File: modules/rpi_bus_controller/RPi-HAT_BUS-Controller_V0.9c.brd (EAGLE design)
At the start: 65 x 56 mm, 77 parts, among them IC1 MC34063AD, IC2 ADUM1201ARZ, IC3 P89LPC922FDH,512FDH, IC4 24LC-I/OT, IC5 LPC1115, Q1 ASF1, Q4 ASFL, T1 BC856, T2 BCP52, T3 BC847

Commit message: Finalize Raspi HAT Dual MCU board
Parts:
- removed C11: 10n, rcl:C1206
- removed C15: 100n, rcl:C1206
- added C51: 10n, rcl:C1206
- added C55: 100n, rcl:C1206
- moved C8 0.15 mm to (11.9, 14.6)
- renumbered C12 to C52, C13 to C53, C14 to C54, C20 to C50, C21 to C56, C22 to C57, D10 to D51, D9 to D50, R21 to R51, R22 to R52, R23 to R53, R24 to R54, R28 to R58, R29 to R59, R30 to R50
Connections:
- net +3V3/2: now also C51.2, C55.2; no longer C11.2, C15.2
- net GND/2: now also C51.1, C55.1; no longer C11.1, C15.1
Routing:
- net +3V3/2: track 164.9 -> 167.6 mm
- net GND/2: track 95.2 -> 96.8 mm, vias 49 -> 52
- net GND: vias 10 -> 41
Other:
- board text added: "Selfbus RPi HAT Dual 1.0"
- board text added: "sh"

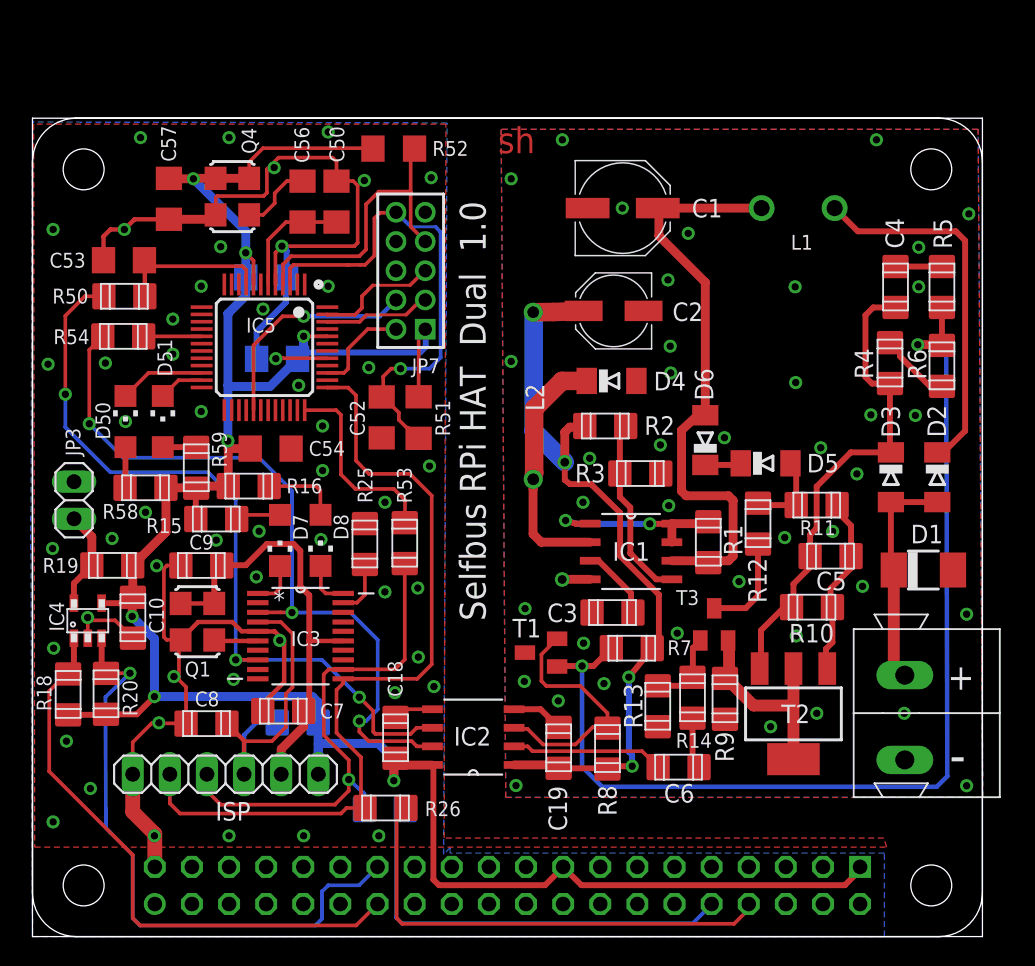
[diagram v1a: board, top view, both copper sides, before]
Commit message: gnd via drill to 0.3mm, place separate bstop over this drills
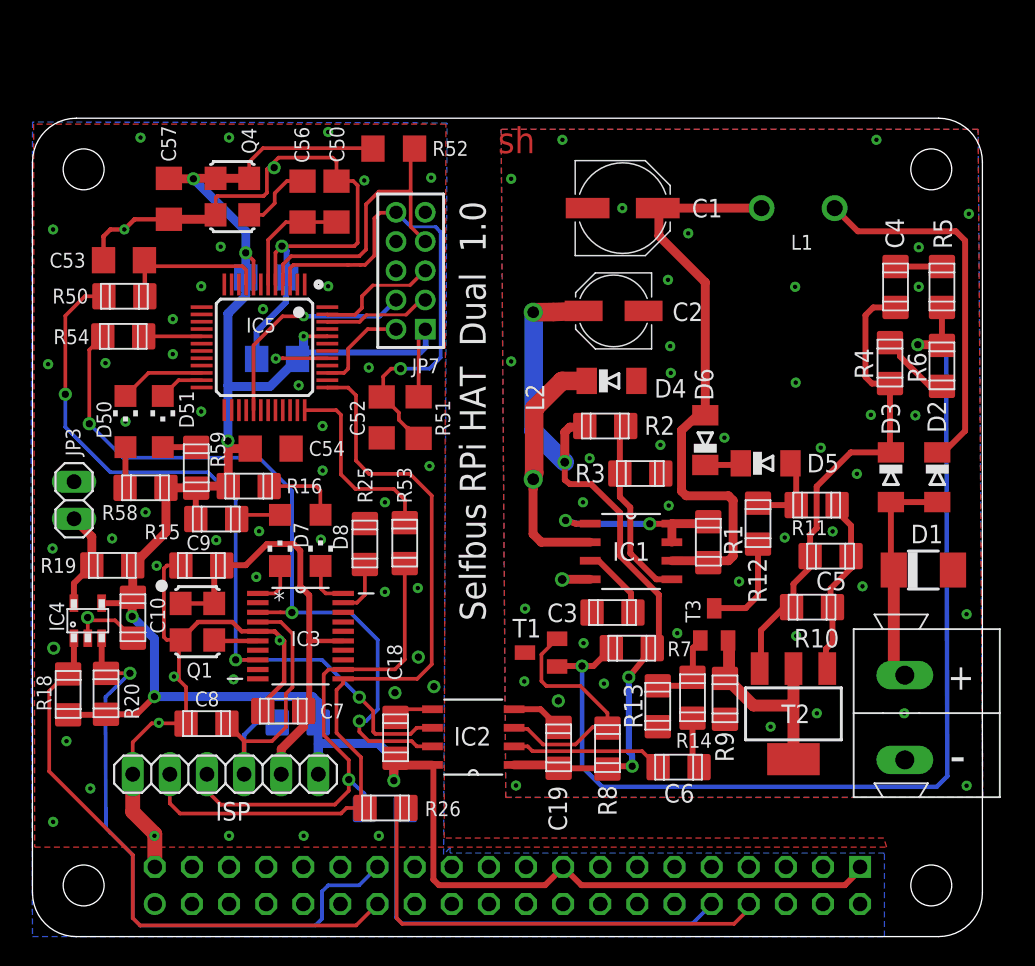
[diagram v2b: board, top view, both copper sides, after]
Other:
- outline, holes or cut-outs redrawn

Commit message: routing vorschlag alle gerouted, noch drc fehler
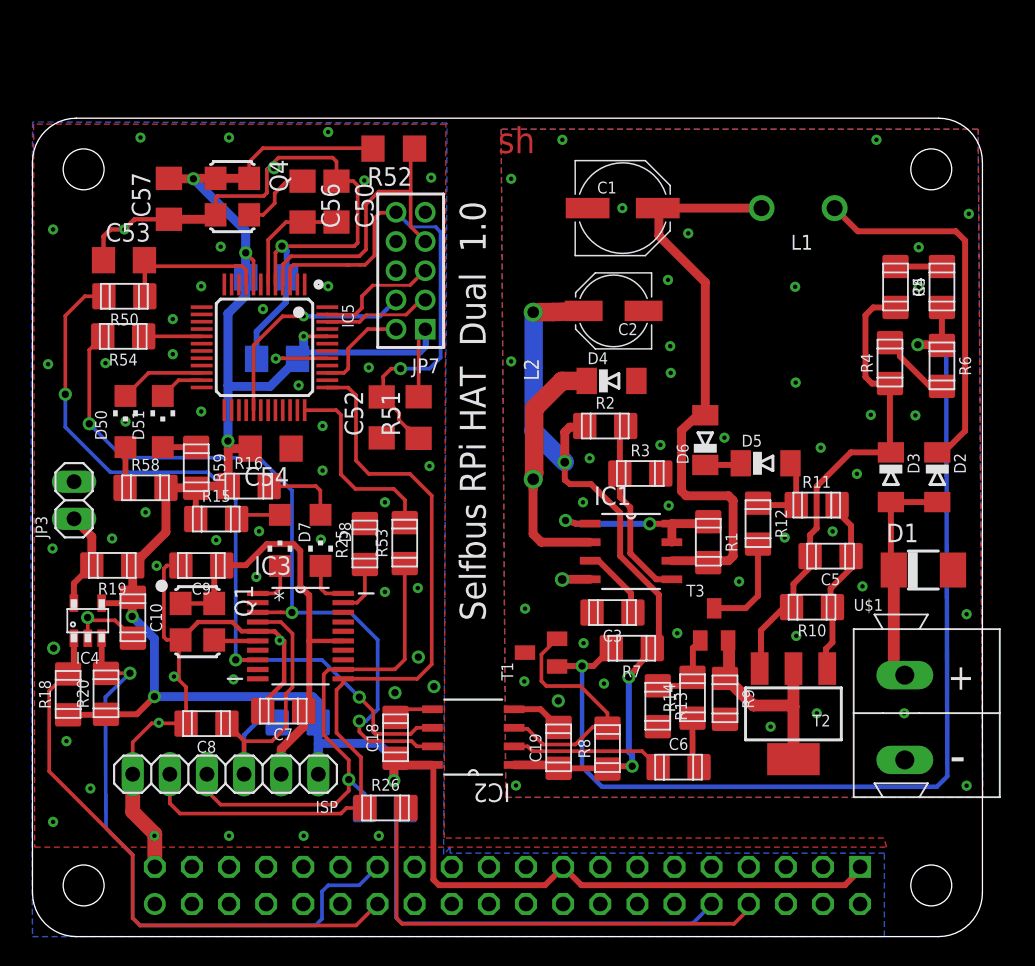
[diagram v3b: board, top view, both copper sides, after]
